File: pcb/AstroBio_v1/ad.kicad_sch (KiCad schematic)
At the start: 47 parts, among them J1 POWER 24V, J10 NTC 10k 3950, J12 HEIGHT_SENSOR2, J13 HEIGHT_SENSOR2, J2 Nema17, J3 MS1, J4 MS2, J5 MS2, J6 MS2, J7 FLOW_SENSOR, J8 SERVO, J9 PH_MODUL, U1 ESP32-DevKitC, U2 TBA2-0511, U3 LM3940, U4 LM358

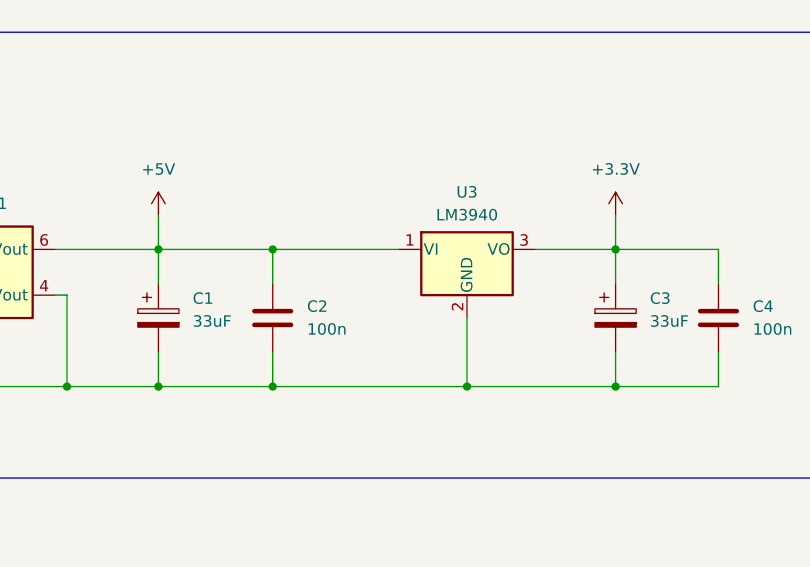
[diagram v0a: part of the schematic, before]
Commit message: change the LDO for a smaller one
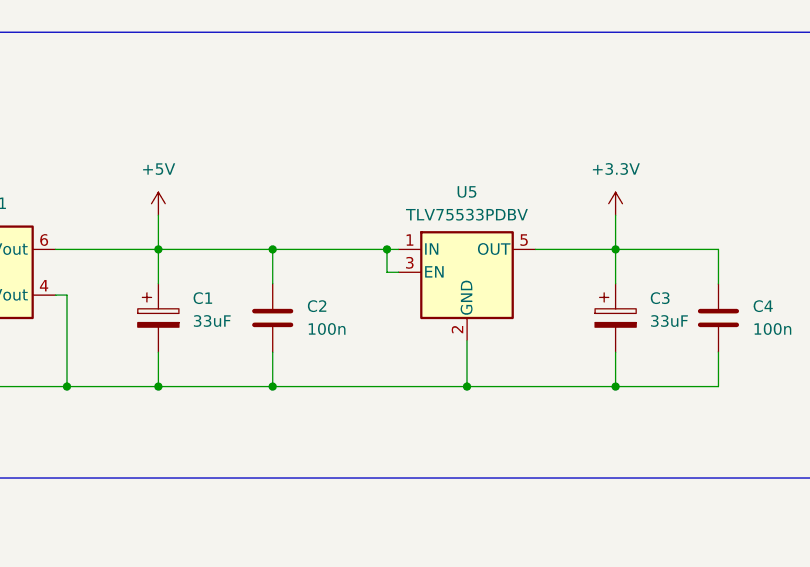
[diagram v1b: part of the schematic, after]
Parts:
- removed U3: LM3940, Package_TO_SOT_THT:TO-220-3_Vertical, symbol Regulator_Linear:LM7805_TO220
- added U5: TLV75533PDBV, Package_TO_SOT_SMD:SOT-23-5, symbol Regulator_Linear:TLV75533PDBV
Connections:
- net +3.3V: now also U5.5 (OUT)
- net +5V: now also U5.1 (IN), U5.3 (EN)
- net GND: now also U5.2 (GND)
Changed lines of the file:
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@@
 	)
 	(junction
-		(at 111.76 40.64)
+		(at 124.46 40.64)
 		(diameter 0)
 		(color 0 0 0 0)
@@
 	)
 	(junction
-		(at 133.35 55.88)
-		(diameter 0)
-		(color 0 0 0 0)
-	)
-	(junction
 		(at 43.18 40.64)
 		(diameter 0)
@@
 	)
 	(junction
+		(at 111.76 40.64)
+		(diameter 0)
+		(color 0 0 0 0)
+	)
+	(junction
 		(at 107.95 222.25)
 		(diameter 0)
@@
 	)
 	(junction
+		(at 133.35 55.88)
+		(diameter 0)
+		(color 0 0 0 0)
+	)
+	(junction
 		(at 275.59 21.59)
 		(diameter 0)
@@
 	(wire
 		(pts
+			(xy 124.46 40.64) (xy 125.73 40.64)
+		)
+		(stroke
+			(width 0)
+			(type default)
+		)
+	)
+	(wire
+		(pts
 			(xy 59.69 219.71) (xy 59.69 222.25)
 		)
@@
 	(wire
 		(pts
-			(xy 111.76 40.64) (xy 125.73 40.64)
+			(xy 111.76 40.64) (xy 124.46 40.64)
 		)
 		(stroke
@@
 	(wire
 		(pts
+			(xy 125.73 43.18) (xy 124.46 43.18)
+		)
+		(stroke
+			(width 0)
+			(type default)
+		)
+	)
+	(wire
+		(pts
 			(xy 72.39 234.95) (xy 92.71 234.95)
 		)
@@
 	(wire
 		(pts
+			(xy 124.46 43.18) (xy 124.46 40.64)
+		)
+		(stroke
+			(width 0)
+			(type default)
+		)
+	)
+	(wire
+		(pts
 			(xy 59.69 217.17) (xy 59.69 219.71)
 		)
@@
 	(wire
 		(pts
-			(xy 133.35 48.26) (xy 133.35 55.88)
+			(xy 133.35 50.8) (xy 133.35 55.88)
 		)
 		(stroke
@@
 	)
 	(symbol
-		(lib_id "power:GND")
-		(at 309.88 69.85 90)
+		(lib_id "Regulator_Linear:TLV75533PDBV")
+		(at 133.35 43.18 0)
 		(unit 1)
 		(body_style 1)
@@
 		(dnp no)
 		(fields_autoplaced yes)
-		(property "Reference" "#PWR07"
-			(at 316.23 69.85 0)
-			(hide yes)
+		(property "Reference" "U5"
+			(at 133.35 34.29 0)
 			(show_name no)
 			(do_not_autoplace no)
@@
 			)
 		)
-		(property "Value" "GND"
-			(at 313.69 69.8499 90)
+		(property "Value" "TLV75533PDBV"
+			(at 133.35 36.83 0)
 			(show_name no)
 			(do_not_autoplace no)
@@
 					(size 1.27 1.27)
 				)
-				(justify right)
 			)
 		)
-		(property "Footprint" ""
-			(at 309.88 69.85 0)
+		(property "Footprint" "Package_TO_SOT_SMD:SOT-23-5"
+			(at 133.35 34.925 0)
 			(hide yes)
 			(show_name no)
@@
 				(font
 					(size 1.27 1.27)
+					(italic yes)
 				)
 			)
 		)
-		(property "Datasheet" ""
-			(at 309.88 69.85 0)
+		(property "Datasheet" "http://www.ti.com/lit/ds/symlink/tlv755p.pdf"
+			(at 133.35 41.91 0)
 			(hide yes)
 			(show_name no)
@@
 			)
 		)
-		(property "Description" "Power symbol creates a global label with name \"GND\" , ground"
-			(at 309.88 69.85 0)
+		(property "Description" "500mA Low Dropout Voltage Regulator, Fixed Output 3.3V, SOT-23-5"
+			(at 133.35 43.18 0)
 			(hide yes)
 			(show_name no)
@@
 			)
 		)
+		(pin "3"
+		)
+		(pin "2"
+		)
+		(pin "4"
+		)
 		(pin "1"
 		)
+		(pin "5"
+		)
 		(instances
 			(project "ad"
 				(path "/de0356da-848d-4af9-ae4e-f0143557b5d0"
-					(reference "#PWR07")
+					(reference "U5")
 					(unit 1)
 				)
@@
 	)
 	(symbol
-		(lib_id "power:+5V")
-		(at 99.06 36.83 0)
+		(lib_id "power:GND")
+		(at 309.88 69.85 90)
 		(unit 1)
 		(body_style 1)
@@
 		(dnp no)
 		(fields_autoplaced yes)
-		(property "Reference" "#PWR03"
-			(at 99.06 40.64 0)
+		(property "Reference" "#PWR07"
+			(at 316.23 69.85 0)
 			(hide yes)
 			(show_name no)
@@
 			)
 		)
-		(property "Value" "+5V"
-			(at 99.06 31.75 0)
+		(property "Value" "GND"
+			(at 313.69 69.8499 90)
 			(show_name no)
 			(do_not_autoplace no)
@@
 					(size 1.27 1.27)
 				)
+				(justify right)
 			)
 		)
 		(property "Footprint" ""
-			(at 99.06 36.83 0)
+			(at 309.88 69.85 0)
 			(hide yes)
 			(show_name no)
@@
 		)
 		(property "Datasheet" ""
-			(at 99.06 36.83 0)
+			(at 309.88 69.85 0)
 			(hide yes)
 			(show_name no)
@@
 			)
 		)
-		(property "Description" "Power symbol creates a global label with name \"+5V\""
-			(at 99.06 36.83 0)
+		(property "Description" "Power symbol creates a global label with name \"GND\" , ground"
+			(at 309.88 69.85 0)
 			(hide yes)
 			(show_name no)
@@
 			(project "ad"
 				(path "/de0356da-848d-4af9-ae4e-f0143557b5d0"
-					(reference "#PWR03")
+					(reference "#PWR07")
 					(unit 1)
 				)
@@
 	)
 	(symbol
-		(lib_id "power:GND")
-		(at 114.3 234.95 0)
+		(lib_id "power:+5V")
+		(at 99.06 36.83 0)
 		(unit 1)
 		(body_style 1)
@@
 		(dnp no)
 		(fields_autoplaced yes)
-		(property "Reference" "#PWR026"
-			(at 114.3 241.3 0)
+		(property "Reference" "#PWR03"
+			(at 99.06 40.64 0)
 			(hide yes)
 			(show_name no)
@@
 			)
 		)
-		(property "Value" "GND"
-			(at 114.3 240.03 0)
+		(property "Value" "+5V"
+			(at 99.06 31.75 0)
 			(show_name no)
 			(do_not_autoplace no)
@@
 		)
 		(property "Footprint" ""
-			(at 114.3 234.95 0)
+			(at 99.06 36.83 0)
 			(hide yes)
 			(show_name no)
@@
 		)
 		(property "Datasheet" ""
-			(at 114.3 234.95 0)
+			(at 99.06 36.83 0)
 			(hide yes)
 			(show_name no)
@@
 			)
 		)
-		(property "Description" "Power symbol creates a global label with name \"GND\" , ground"
-			(at 114.3 234.95 0)
+		(property "Description" "Power symbol creates a global label with name \"+5V\""
+			(at 99.06 36.83 0)
 			(hide yes)
 			(show_name no)
@@
 			(project "ad"
 				(path "/de0356da-848d-4af9-ae4e-f0143557b5d0"
-					(reference "#PWR026")
+					(reference "#PWR03")
 					(unit 1)
 				)
@@
 	(symbol
 		(lib_id "power:GND")
-		(at 240.03 101.6 180)
+		(at 114.3 234.95 0)
 		(unit 1)
 		(body_style 1)
@@
 		(dnp no)
 		(fields_autoplaced yes)
-		(property "Reference" "#PWR019"
-			(at 240.03 95.25 0)
+		(property "Reference" "#PWR026"
+			(at 114.3 241.3 0)
 			(hide yes)
 			(show_name no)
@@
 		)
 		(property "Value" "GND"
-			(at 240.03 96.52 0)
+			(at 114.3 240.03 0)
 			(show_name no)
 			(do_not_autoplace no)
@@
 		)
 		(property "Footprint" ""
-			(at 240.03 101.6 0)
+			(at 114.3 234.95 0)
 			(hide yes)
 			(show_name no)
@@
 		)
 		(property "Datasheet" ""
-			(at 240.03 101.6 0)
+			(at 114.3 234.95 0)
 			(hide yes)
 			(show_name no)
@@
 		)
 		(property "Description" "Power symbol creates a global label with name \"GND\" , ground"
-			(at 240.03 101.6 0)
+			(at 114.3 234.95 0)
 			(hide yes)
 			(show_name no)
@@
 			(project "ad"
 				(path "/de0356da-848d-4af9-ae4e-f0143557b5d0"
-					(reference "#PWR019")
+					(reference "#PWR026")
 					(unit 1)
 				)
@@
 	)
 	(symbol
-		(lib_id "Regulator_Linear:LM7805_TO220")
-		(at 133.35 40.64 0)
+		(lib_id "power:GND")
+		(at 240.03 101.6 180)
 		(unit 1)
 		(body_style 1)
@@
 		(dnp no)
 		(fields_autoplaced yes)
-		(property "Reference" "U3"
-			(at 133.35 34.29 0)
+		(property "Reference" "#PWR019"
+			(at 240.03 95.25 0)
+			(hide yes)
 			(show_name no)
 			(do_not_autoplace no)
@@
 			)
 		)
-		(property "Value" "LM3940"
-			(at 133.35 36.83 0)
+		(property "Value" "GND"
+			(at 240.03 96.52 0)
 			(show_name no)
 			(do_not_autoplace no)
@@
 			)
 		)
-		(property "Footprint" "Package_TO_SOT_THT:TO-220-3_Vertical"
-			(at 133.35 34.925 0)
+		(property "Footprint" ""
+			(at 240.03 101.6 0)
 			(hide yes)
 			(show_name no)
@@
 				(font
 					(size 1.27 1.27)
-					(italic yes)
 				)
 			)
 		)
-		(property "Datasheet" "https://www.onsemi.cn/PowerSolutions/document/MC7800-D.PDF"
-			(at 133.35 41.91 0)
+		(property "Datasheet" ""
+			(at 240.03 101.6 0)
 			(hide yes)
 			(show_name no)
@@
 			)
 		)
-		(property "Description" "Positive 1A 35V Linear Regulator, Fixed Output 5V, TO-220"
-			(at 133.35 40.64 0)
+		(property "Description" "Power symbol creates a global label with name \"GND\" , ground"
+			(at 240.03 101.6 0)
 			(hide yes)
 			(show_name no)
@@
 			)
 		)
-		(pin "3"
-		)
 		(pin "1"
 		)
-		(pin "2"
-		)
 		(instances
 			(project "ad"
 				(path "/de0356da-848d-4af9-ae4e-f0143557b5d0"
-					(reference "U3")
+					(reference "#PWR019")
 					(unit 1)
 				)
